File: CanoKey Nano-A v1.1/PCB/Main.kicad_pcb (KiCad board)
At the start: 2 copper layers, 49.8 x 20.3 mm, 32 parts, among them J1 USB_A_PCB, U1 FM11NC08S, U2 USBLC6-2SC6, U3 STM32L432KCUx, U4 AP7331-33SNG-7

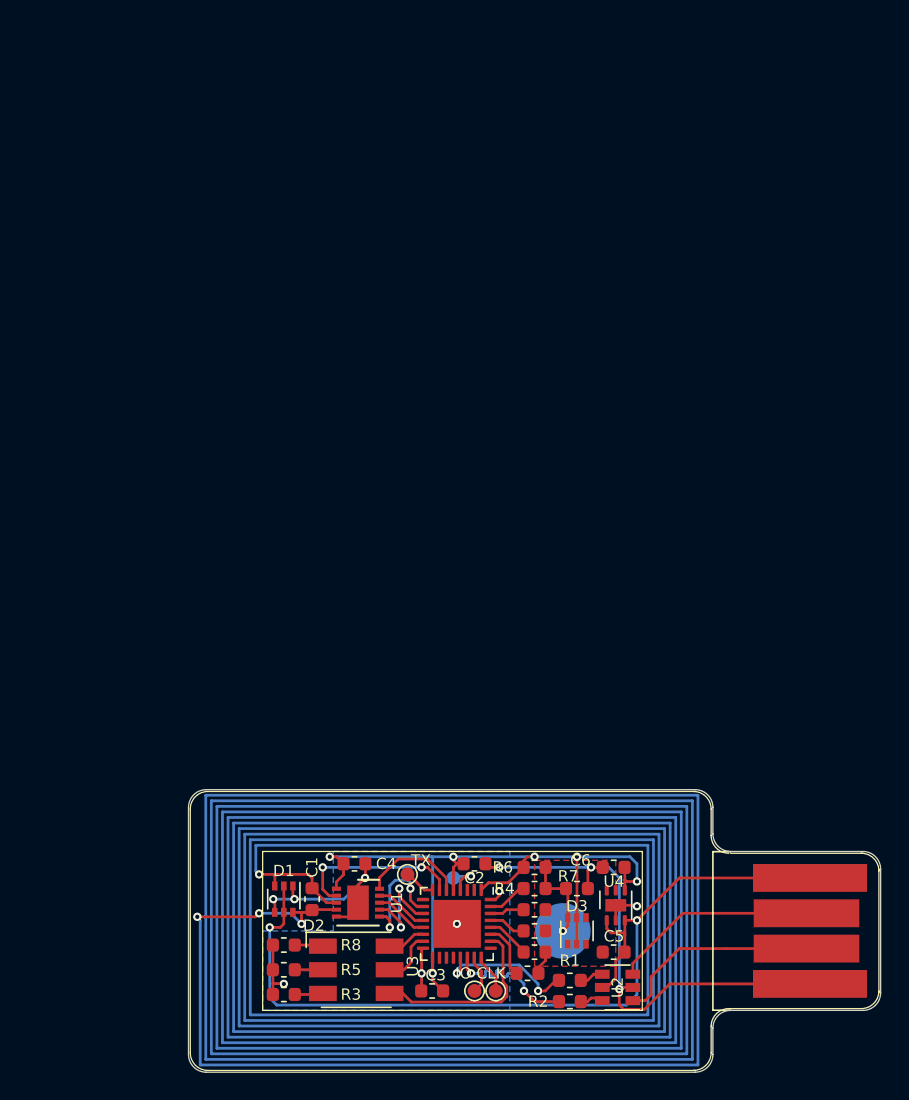
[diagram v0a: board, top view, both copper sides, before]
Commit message: compact PCB
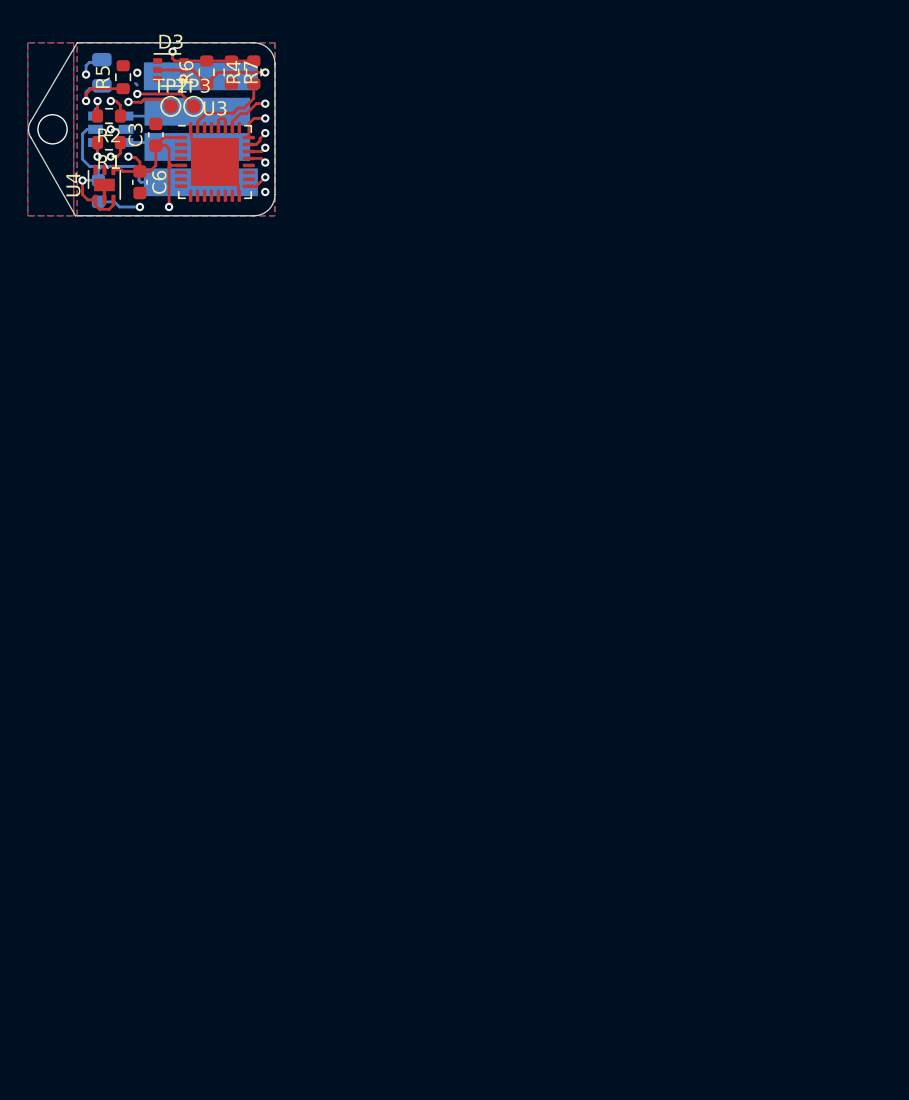
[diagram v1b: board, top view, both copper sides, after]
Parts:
- removed C1: ~, Capacitor_SMD:C_0603_1608Metric
- removed C2, C4: 100n, Capacitor_SMD:C_0603_1608Metric
- removed D2: MHP5050RGBDT, LED_SMD:LED_RGB_5050-6
- removed G***: LOGO, MAS_Package_nostd:CanoKeys
- removed R10, R11, R12, R9: ~, Resistor_SMD:R_0603_1608Metric
- removed R3, R8: 2.2k, Resistor_SMD:R_0603_1608Metric
- removed TP1, TP5: TestPoint, TestPoint:TestPoint_Pad_D1.0mm
- removed TP4: TestPoint, TestPoint:TestPoint_Pad_D4.0mm
- removed U1: FM11NC08S, Package_DFN_QFN:DFN-10-1EP_3x3mm_P0.5mm_EP1.55x2.48mm
- C5, J1, U2: moved to B.Cu
- D1: value BAT54XY -> LED_G; footprint Package_TO_SOT_SMD:SOT-363_SC-70-6 -> Diode_SMD:D_0805_2012Metric; moved to B.Cu
- moved J1 72.4 mm to (132.1, 43.9)
- moved R2 71.8 mm to (131.2, 43.0), turned to 180 degrees
- moved U2 71.7 mm to (131.3, 43.9)
- moved R1 68.8 mm to (131.2, 44.9), turned to 180 degrees
- moved D3 68.5 mm to (135.6, 39.7), turned to 0 degrees
- moved TP2 67.3 mm to (135.6, 42.3), turned to 0 degrees
- moved TP3 67.2 mm to (137.3, 42.3), turned to 0 degrees
- moved C5 66.1 mm to (130.4, 48.4), turned to 270 degrees
- moved R5 65.2 mm to (132.2, 40.2), turned to 90 degrees
- moved C3 64.7 mm to (134.6, 44.3), turned to 90 degrees
- moved R7 63.7 mm to (140.0, 39.9), turned to 270 degrees
- moved U4 63.5 mm to (130.9, 47.9)
- moved R4 62.1 mm to (141.6, 39.9), turned to 90 degrees
- moved R6 61.8 mm to (138.2, 39.9), turned to 90 degrees
- moved D1 60.9 mm to (130.7, 39.9), turned to 90 degrees
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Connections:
- D1 pad 1: GND -> Net-(D1-Pad1)
- D1 pad 2: +5V -> /LEDG
- R5 pad 1: Net-(D2-Pad2) -> Net-(D1-Pad1)
- U3 pad 14: /LEDB -> Net-(U3-Pad14)
- U3 pad 15: /LEDG -> Net-(U3-Pad15)
- U3 pad 26: /LEDR -> /LEDG
- U3 pad 27: /PB4 -> Net-(U3-Pad27)
- U3 pad 28: /PB5 -> Net-(U3-Pad27)
- U3 pad 29: /PB6 -> Net-(U3-Pad29)
- U3 pad 30: /PB7 -> Net-(U3-Pad30)
- U3 pad 4: /RST -> Net-(U3-Pad4)
- U3 pad 8: /DBG_TX -> Net-(U3-Pad8)
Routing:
- net /L1: track 972.7 -> 0.00 mm, vias 4 -> 0
- net GND: track 66.3 -> 12.8 mm, vias 11 -> 4
- net +5V: track 65.0 -> 20.6 mm, vias 2 -> 1
- net /LEDG: track 3.91 -> 19.7 mm, vias 0 -> 2
- net /SWCLK: track 2.82 -> 16.7 mm, vias 0 -> 2
- net /LEDR: track 13.6 -> 0.00 mm
- net Net-(D3-Pad6): track 6.25 -> 19.5 mm, vias 1 -> 2
- net /SWDIO: track 2.81 -> 16.1 mm, vias 0 -> 2
- net /V_RF: track 12.3 -> 0.00 mm, vias 2 -> 0
- net Net-(J1-Pad3): track 16.1 -> 5.13 mm
- net Net-(J1-Pad2): track 16.0 -> 5.13 mm
- net +3V3: track 55.6 -> 46.9 mm, vias 6 -> 4
- net /SSN: track 8.43 -> 0.00 mm, vias 2 -> 0
- net /SCLK: track 7.90 -> 0.00 mm, vias 2 -> 0
- net /IRQN: track 7.59 -> 0.00 mm
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- added copper zone on In1.Cu, net GND
- added copper zone on In2.Cu, net GND
- added copper zone on B.Cu, net Net-(D3-Pad6)
- added copper zone on F.Cu, net Net-(D3-Pad6)
- added copper zone on In1.Cu, net Net-(D3-Pad6)
- added copper zone on In2.Cu, net Net-(D3-Pad6)
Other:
- board size 49.8 x 20.3 mm -> 17.7 x 12.4 mm
- copper layers 2 -> 4
- net class Power added: clearance 0.2, trace_width 0.2, via_dia 0.6, via_drill 0.3
- rule pad_to_mask_clearance: 0.05 -> 0
- rule via_min_size: 0.4 -> 0.3
- board text removed: "CLK"
- board text removed: "CanoKey"
- board text removed: "IO"
- board text removed: "NFC-A v2"
- board text removed: "RST"
- board text removed: "TX"
